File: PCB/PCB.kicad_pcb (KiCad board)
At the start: 2 copper layers, 18 x 13 mm, 6 parts, among them J1 USB_C_Receptacle_PowerOnly_6P

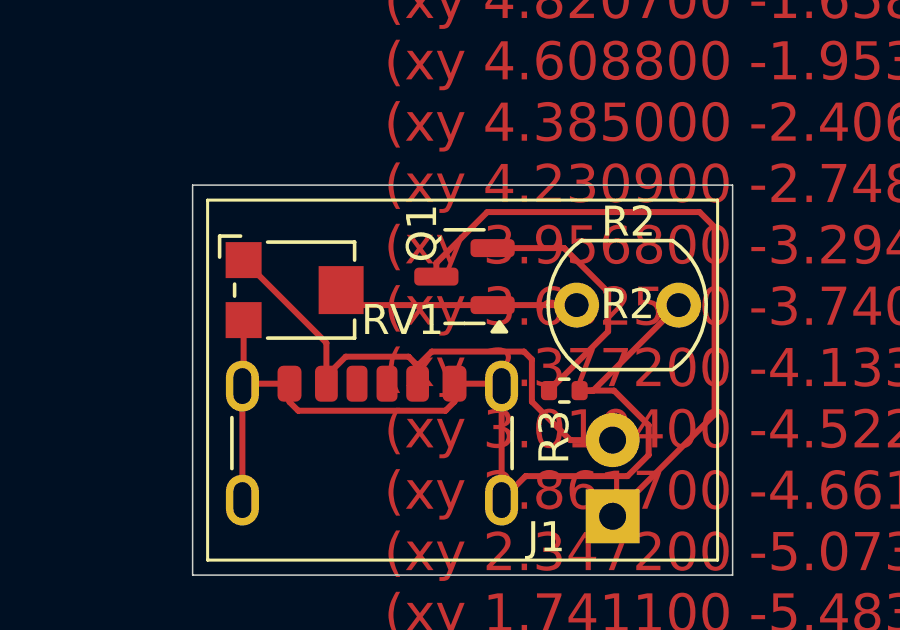
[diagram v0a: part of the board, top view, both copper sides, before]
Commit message: Add and route CC 5k1Ω resistors
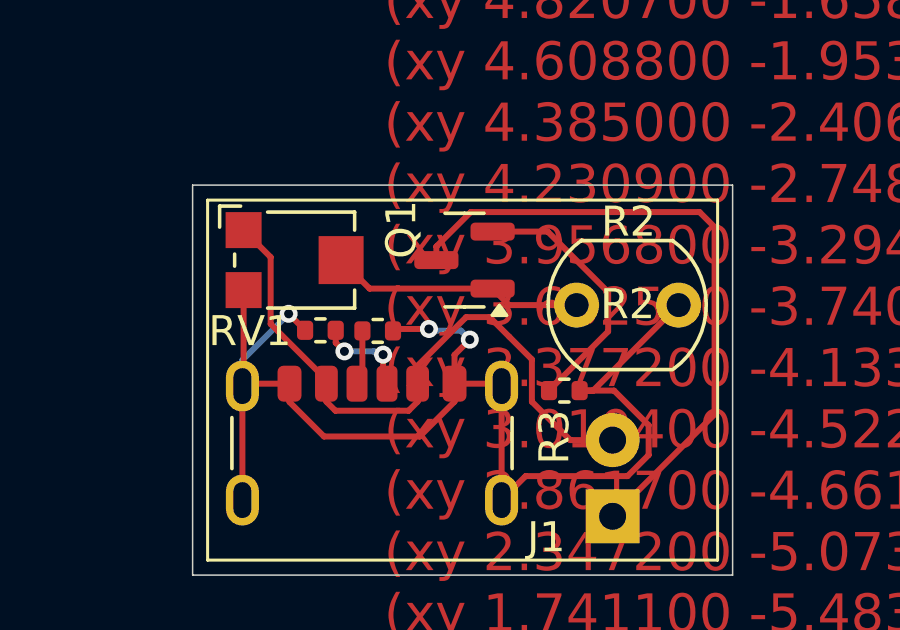
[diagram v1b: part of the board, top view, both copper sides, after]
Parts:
- added R1: 5k1Ω, Resistor_SMD:R_0402_1005Metric, F.Cu at (155.8, 100.8)
- added R4: 5k1Ω, Resistor_SMD:R_0402_1005Metric, F.Cu at (157.7, 100.9)
- moved RV1 1.00 mm to (155.0, 98.5)
- moved Q1 0.55 mm to (160.6, 98.5)
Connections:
- J1 pad A5: unconnected-(J1-CC1-PadA5) -> Net-(J1-CC1)
- J1 pad B5: unconnected-(J1-CC2-PadB5) -> Net-(J1-CC2)
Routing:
- net Net-(J1-SHIELD): track 33.8 -> 43.7 mm, vias 0 -> 3
- net Net-(J1-CC2): track 0.00 -> 3.18 mm, vias 0 -> 2
- net Net-(D1-A): track 18.3 -> 21.3 mm
- net Net-(J1-CC1): track 0.00 -> 1.83 mm
